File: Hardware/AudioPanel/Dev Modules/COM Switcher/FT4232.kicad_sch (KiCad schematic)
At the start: 81 parts, among them J601 PC1_COM, J602 PC2_COM, J603 PC3_COM, J604 PC4_COM, J605 2.54mm, Q601 BCM857BS, U601 FT4232H, U602 93LCxxA, Y601 12MHz

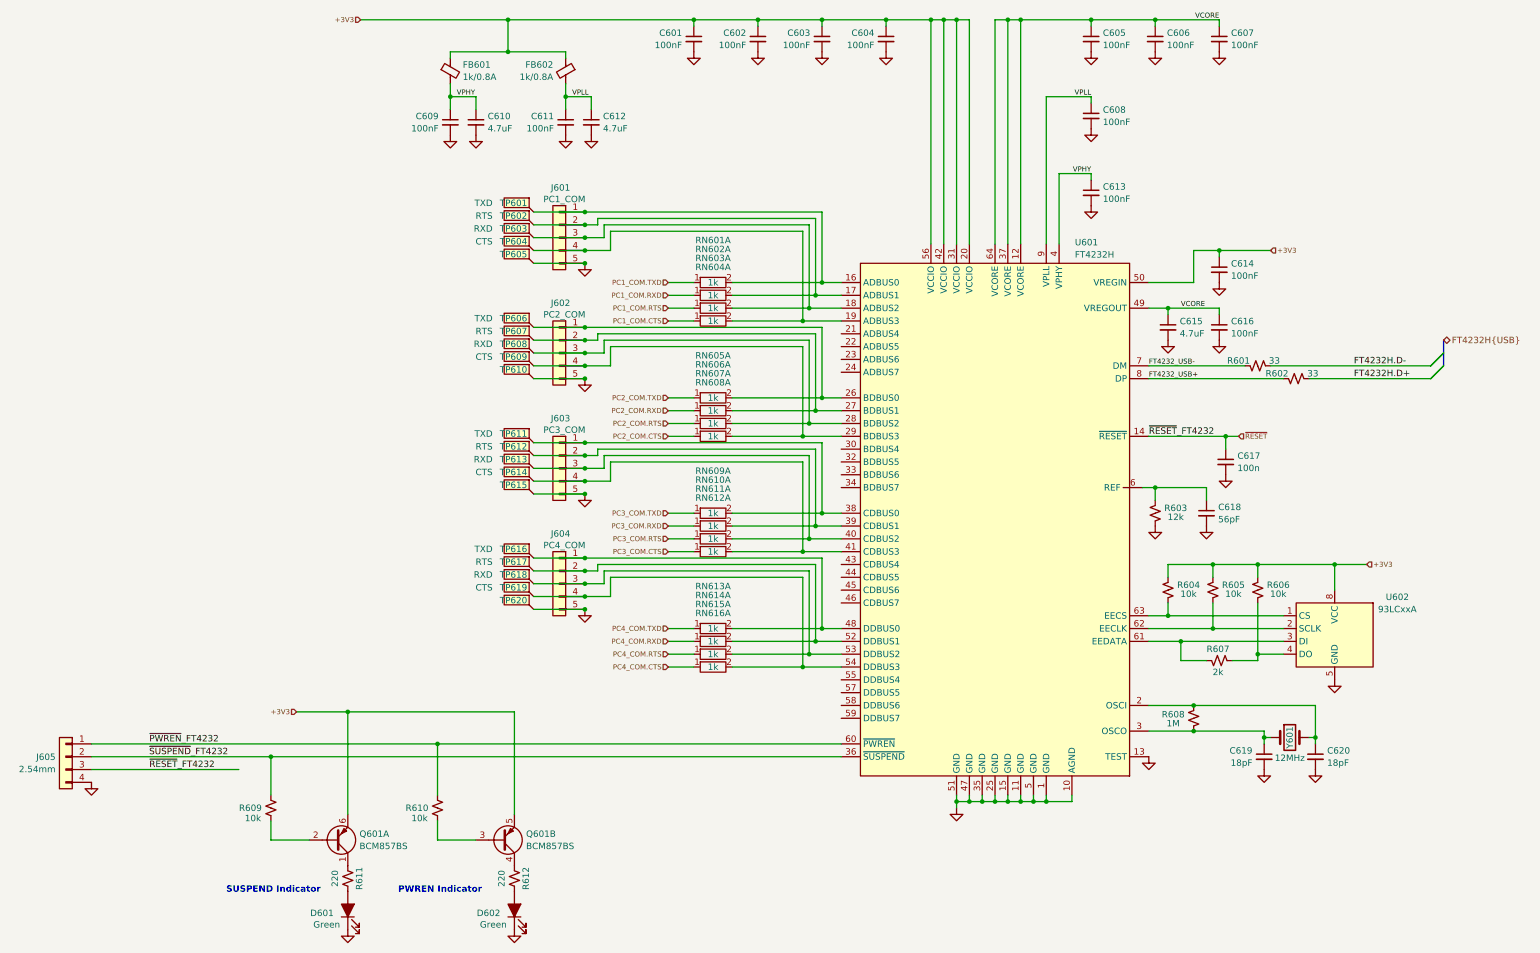
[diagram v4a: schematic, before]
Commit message: Changed passives to Worthington footprints
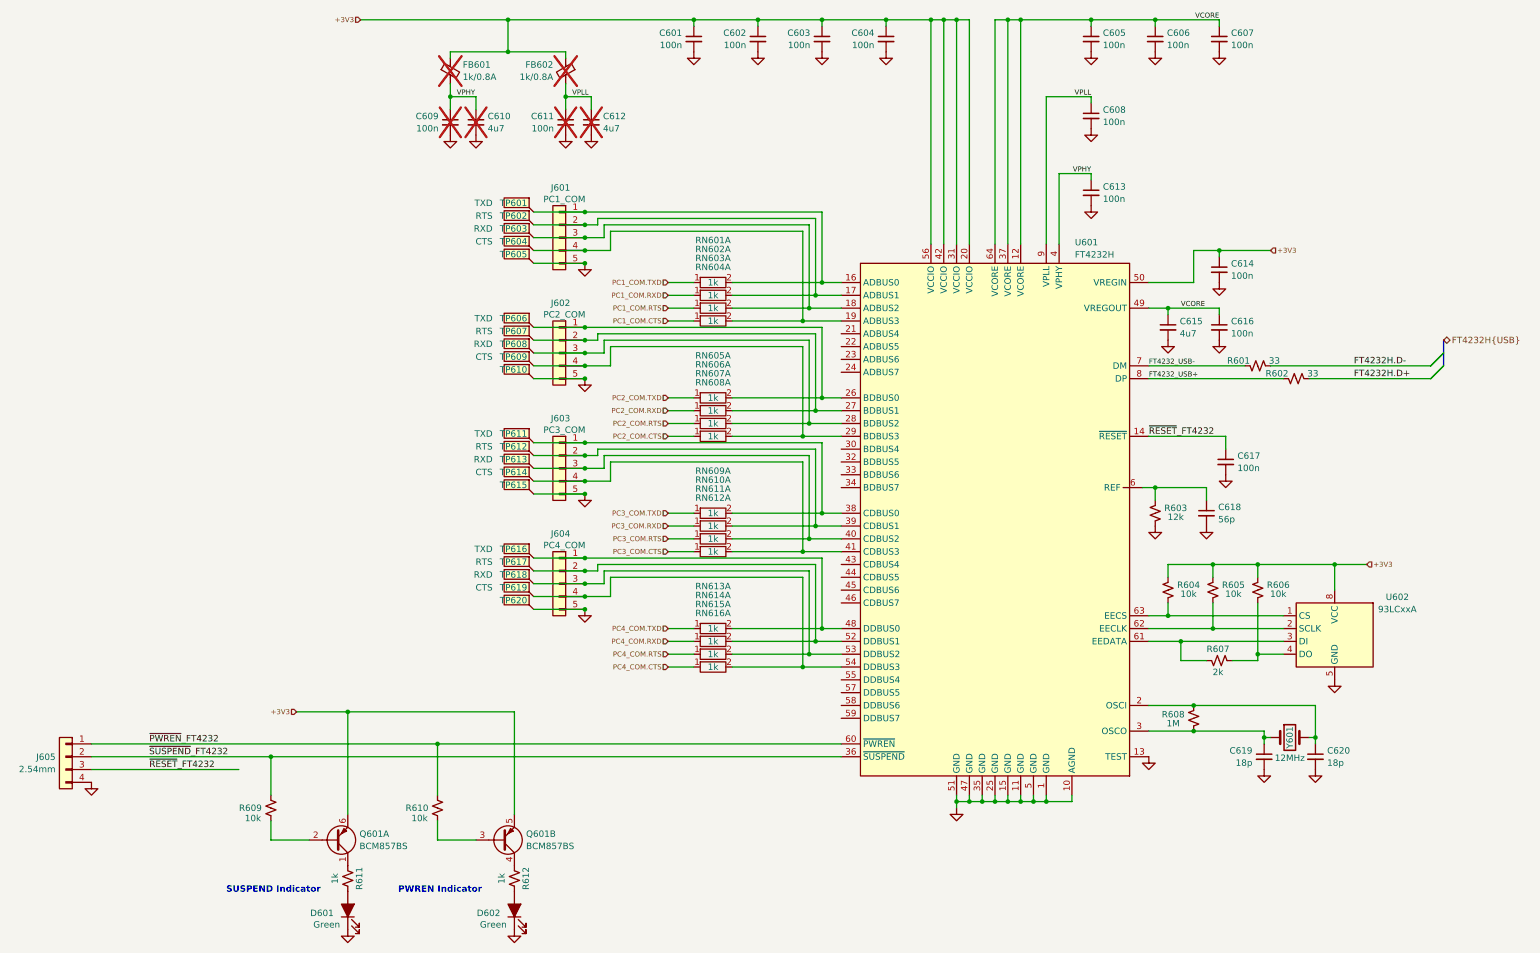
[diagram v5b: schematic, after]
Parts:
- C601, C602, C603, C604, C605, C606, C607, C608, C613, C614, C616: value 100nF -> 100n; footprint Capacitor_SMD:C_0402_1005Metric -> Libraries:Worthington_C_0402
- C609, C611: value 100nF -> 100n; footprint Capacitor_SMD:C_0402_1005Metric -> Libraries:Worthington_C_0402; now not fitted
- C610: value 4.7uF -> 4u7; footprint Capacitor_SMD:C_0603_1608Metric -> Libraries:Worthington_C_0603; now not fitted
- C612: value 4.7uF -> 4u7; footprint Capacitor_SMD:C_0603_1608Metric -> Libraries:Worthington_C_0402; now not fitted
- C615: value 4.7uF -> 4u7; footprint Capacitor_SMD:C_0603_1608Metric -> Libraries:Worthington_C_0603
- C617: footprint Capacitor_SMD:C_0402_1005Metric -> Libraries:Worthington_C_0402
- C618: value 56pF -> 56p; footprint Capacitor_SMD:C_0402_1005Metric -> Libraries:Worthington_C_0402
- C619, C620: value 18pF -> 18p; footprint Capacitor_SMD:C_0402_1005Metric -> Libraries:Worthington_C_0402
- FB601, FB602: now not fitted
- R601, R602, R603, R604, R605, R606, R607, R608, R609, R610: footprint Resistor_SMD:R_0402_1005Metric -> Libraries:Worthington_R_0402
- R611, R612: value 220 -> 1k; footprint Resistor_SMD:R_0402_1005Metric -> Libraries:Worthington_R_0402
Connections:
- net ~{RESET} renamed ~{RESET}_FT4232
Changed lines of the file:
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@@
 	)
 	(junction
-		(at 323.85 115.57)
-		(diameter 0)
-		(color 0 0 0 0)
-	)
-	(junction
 		(at 322.58 78.74)
 		(diameter 0)
@@
 	(wire
 		(pts
-			(xy 326.39 115.57) (xy 323.85 115.57)
-		)
-		(stroke
-			(width 0)
-			(type default)
-		)
-	)
-	(wire
-		(pts
 			(xy 256.54 33.02) (xy 265.43 33.02)
 		)
@@
 		)
 	)
-	(hierarchical_label "~{RESET}"
-		(shape input)
-		(at 326.39 115.57 0)
-		(effects
-			(font
-				(size 1 1)
-			)
-			(justify left)
-		)
-	)
 	(hierarchical_label "PC3_COM.TXD"
 		(shape input)
@@
 			)
 		)
-		(property "Footprint" "Resistor_SMD:R_0402_1005Metric"
+		(property "Footprint" "Libraries:Worthington_R_0402"
 			(at 312.42 146.05 0)
 			(effects
@@
 			)
 		)
-		(property "Footprint" "Resistor_SMD:R_0402_1005Metric"
+		(property "Footprint" "Libraries:Worthington_R_0402"
 			(at 321.31 146.05 0)
 			(effects
@@
 			)
 		)
-		(property "Value" "100nF"
+		(property "Value" "100n"
 			(at 216.1159 38.0484 0)
 			(effects
@@
 			)
 		)
-		(property "Footprint" "Capacitor_SMD:C_0402_1005Metric"
+		(property "Footprint" "Libraries:Worthington_C_0402"
 			(at 218.44 36.83 0)
 			(effects
@@
 			)
 		)
-		(property "Value" "100nF"
+		(property "Value" "100n"
 			(at 228.8159 38.0484 0)
 			(effects
@@
 			)
 		)
-		(property "Footprint" "Capacitor_SMD:C_0402_1005Metric"
+		(property "Footprint" "Libraries:Worthington_C_0402"
 			(at 231.14 36.83 0)
 			(effects
@@
 		(in_bom yes)
 		(on_board yes)
-		(dnp no)
+		(dnp yes)
 		(fields_autoplaced yes)
 		(property "Reference" "FB601"
@@
 			)
 		)
-		(property "Footprint" "Resistor_SMD:R_0402_1005Metric"
+		(property "Footprint" "Libraries:Worthington_R_0402"
 			(at 167.64 189.23 0)
 			(effects
@@
 			)
 		)
-		(property "Value" "220"
+		(property "Value" "1k"
 			(at 147.32 203.2 90)
 			(effects
@@
 			)
 		)
-		(property "Footprint" "Resistor_SMD:R_0402_1005Metric"
+		(property "Footprint" "Libraries:Worthington_R_0402"
 			(at 149.86 203.2 0)
 			(effects
@@
 		(in_bom yes)
 		(on_board yes)
-		(dnp no)
+		(dnp yes)
 		(property "Reference" "C610"
 			(at 177.5841 52.1341 0)
@@
 			)
 		)
-		(property "Value" "4.7uF"
+		(property "Value" "4u7"
 			(at 177.5841 54.5584 0)
 			(effects
@@
 			)
 		)
-		(property "Footprint" "Capacitor_SMD:C_0603_1608Metric"
+		(property "Footprint" "Libraries:Worthington_C_0603"
 			(at 175.26 53.34 0)
 			(effects
@@
 			)
 		)
-		(property "Value" "100nF"
+		(property "Value" "100n"
 			(at 324.9041 95.1984 0)
 			(effects
@@
 			)
 		)
-		(property "Footprint" "Capacitor_SMD:C_0402_1005Metric"
+		(property "Footprint" "Libraries:Worthington_C_0402"
 			(at 322.58 93.98 0)
 			(effects
@@
 			)
 		)
-		(property "Value" "18pF"
+		(property "Value" "18p"
 			(at 343.9541 180.2884 0)
 			(effects
@@
 			)
 		)
-		(property "Footprint" "Capacitor_SMD:C_0402_1005Metric"
+		(property "Footprint" "Libraries:Worthington_C_0402"
 			(at 341.63 179.07 0)
 			(effects
@@
 			)
 		)
-		(property "Footprint" "Resistor_SMD:R_0402_1005Metric"
+		(property "Footprint" "Libraries:Worthington_R_0402"
 			(at 337.82 104.14 0)
 			(effects
@@
 		(in_bom yes)
 		(on_board yes)
-		(dnp no)
+		(dnp yes)
 		(property "Reference" "C611"
 			(at 190.7159 52.1341 0)
@@
 			)
 		)
-		(property "Value" "100nF"
+		(property "Value" "100n"
 			(at 190.7159 54.5584 0)
 			(effects
@@
 			)
 		)
-		(property "Footprint" "Capacitor_SMD:C_0402_1005Metric"
+		(property "Footprint" "Libraries:Worthington_C_0402"
 			(at 193.04 53.34 0)
 			(effects
@@
 			)
 		)
-		(property "Footprint" "Resistor_SMD:R_0402_1005Metric"
+		(property "Footprint" "Libraries:Worthington_R_0402"
 			(at 309.88 130.81 0)
 			(effects
@@
 			)
 		)
-		(property "Footprint" "Capacitor_SMD:C_0402_1005Metric"
+		(property "Footprint" "Libraries:Worthington_C_0402"
 			(at 323.85 120.65 0)
 			(effects
@@
 			)
 		)
-		(property "Footprint" "Resistor_SMD:R_0402_1005Metric"
+		(property "Footprint" "Libraries:Worthington_R_0402"
 			(at 317.5 171.45 0)
 			(effects
@@
 			)
 		)
-		(property "Footprint" "Resistor_SMD:R_0402_1005Metric"
+		(property "Footprint" "Libraries:Worthington_R_0402"
 			(at 330.2 146.05 0)
 			(effects
@@
 		(in_bom yes)
 		(on_board yes)
-		(dnp no)
+		(dnp yes)
 		(property "Reference" "C609"
 			(at 167.8559 52.1341 0)
@@
 			)
 		)
-		(property "Value" "100nF"
+		(property "Value" "100n"
 			(at 167.8559 54.5584 0)
 			(effects
@@
 			)
 		)
-		(property "Footprint" "Capacitor_SMD:C_0402_1005Metric"
+		(property "Footprint" "Libraries:Worthington_C_0402"
 			(at 170.18 53.34 0)
 			(effects
@@
 			)
 		)
-		(property "Value" "56pF"
+		(property "Value" "56p"
 			(at 322.3641 132.0284 0)
 			(effects
@@
 			)
 		)
-		(property "Footprint" "Capacitor_SMD:C_0402_1005Metric"
+		(property "Footprint" "Libraries:Worthington_C_0402"
 			(at 320.04 130.81 0)
 			(effects
@@
 			)
 		)
-		(property "Value" "4.7uF"
+		(property "Value" "4u7"
 			(at 314.7441 95.1984 0)
 			(effects
@@
 			)
 		)
-		(property "Footprint" "Capacitor_SMD:C_0603_1608Metric"
+		(property "Footprint" "Libraries:Worthington_C_0603"
 			(at 312.42 93.98 0)
 			(effects
@@
 			)
 		)
-		(property "Footprint" "Resistor_SMD:R_0402_1005Metric"
+		(property "Footprint" "Libraries:Worthington_R_0402"
 			(at 330.2 101.6 0)
 			(effects
@@
 			)
 		)
-		(property "Value" "220"
+		(property "Value" "1k"
 			(at 180.34 203.2 90)
 			(effects
@@
 			)
 		)
-		(property "Footprint" "Resistor_SMD:R_0402_1005Metric"
+		(property "Footprint" "Libraries:Worthington_R_0402"
 			(at 182.88 203.2 0)
 			(effects
@@
 			)
 		)
-		(property "Value" "18pF"
+		(property "Value" "18p"
 			(at 329.1459 180.2884 0)
 			(effects
@@
 			)
 		)
-		(property "Footprint" "Capacitor_SMD:C_0402_1005Metric"
+		(property "Footprint" "Libraries:Worthington_C_0402"
 			(at 331.47 179.07 0)
 			(effects
@@
 			)
 		)
-		(property "Footprint" "Resistor_SMD:R_0402_1005Metric"
+		(property "Footprint" "Libraries:Worthington_R_0402"
 			(at 134.62 189.23 0)
 			(effects
@@
 			)
 		)
-		(property "Value" "100nF"
+		(property "Value" "100n"
 			(at 299.5041 38.0484 0)
 			(effects
@@
 			)
 		)
-		(property "Footprint" "Capacitor_SMD:C_0402_1005Metric"
+		(property "Footprint" "Libraries:Worthington_C_0402"
 			(at 297.18 36.83 0)
 			(effects
@@
 			)
 		)
-		(property "Value" "100nF"
+		(property "Value" "100n"
 			(at 241.5159 38.0484 0)
 			(effects
@@
 			)
 		)
-		(property "Footprint" "Capacitor_SMD:C_0402_1005Metric"
+		(property "Footprint" "Libraries:Worthington_C_0402"
 			(at 243.84 36.83 0)
 			(effects
@@
 			)
 		)
-		(property "Value" "100nF"
+		(property "Value" "100n"
 			(at 299.5041 68.5284 0)
 			(effects
@@
 			)
 		)
-		(property "Footprint" "Capacitor_SMD:C_0402_1005Metric"
+		(property "Footprint" "Libraries:Worthington_C_0402"
 			(at 297.18 67.31 0)
 			(effects
@@
 		(in_bom yes)
 		(on_board yes)
-		(dnp no)
+		(dnp yes)
 		(property "Reference" "C612"
 			(at 200.4441 52.1341 0)
@@
 			)
 		)
-		(property "Value" "4.7uF"
+		(property "Value" "4u7"
 			(at 200.4441 54.5584 0)
 			(effects
@@
 			)
 		)
-		(property "Footprint" "Capacitor_SMD:C_0603_1608Metric"
+		(property "Footprint" "Libraries:Worthington_C_0402"
 			(at 198.12 53.34 0)
 			(effects
@@
 			)
 		)
-		(property "Value" "100nF"
+		(property "Value" "100n"
 			(at 324.9041 83.7684 0)
 			(effects
@@
 			)
 		)
-		(property "Footprint" "Capacitor_SMD:C_0402_1005Metric"
+		(property "Footprint" "Libraries:Worthington_C_0402"
 			(at 322.58 82.55 0)
 			(effects
@@
 			)
 		)
-		(property "Value" "100nF"
+		(property "Value" "100n"
 			(at 324.9041 38.0484 0)
 			(effects
@@
 			)
 		)
-		(property "Footprint" "Capacitor_SMD:C_0402_1005Metric"
+		(property "Footprint" "Libraries:Worthington_C_0402"
 			(at 322.58 36.83 0)
 			(effects
@@
 		(in_bom yes)
 		(on_board yes)
-		(dnp no)
+		(dnp yes)
 		(property "Reference" "FB602"
 			(at 190.5762 41.9297 0)
@@
 			)
 		)
-		(property "Value" "100nF"
+		(property "Value" "100n"
 			(at 299.5041 53.2884 0)
 			(effects
@@
 			)
 		)
-		(property "Footprint" "Capacitor_SMD:C_0402_1005Metric"
+		(property "Footprint" "Libraries:Worthington_C_0402"
 			(at 297.18 52.07 0)
 			(effects
@@
 			)
 		)
-		(property "Value" "100nF"
+		(property "Value" "100n"
 			(at 312.2041 38.0484 0)
 			(effects
@@
 			)
 		)
-		(property "Footprint" "Capacitor_SMD:C_0402_1005Metric"
+		(property "Footprint" "Libraries:Worthington_C_0402"
 			(at 309.88 36.83 0)
 			(effects
@@
 			)
 		)
-		(property "Footprint" "Resistor_SMD:R_0402_1005Metric"
+		(property "Footprint" "Libraries:Worthington_R_0402"
 			(at 322.58 160.02 0)
 			(effects
@@
 			)
 		)
-		(property "Value" "100nF"
+		(property "Value" "100n"
 			(at 254.2159 38.0484 0)
 			(effects
@@
 			)
 		)
-		(property "Footprint" "Capacitor_SMD:C_0402_1005Metric"
+		(property "Footprint" "Libraries:Worthington_C_0402"
 			(at 256.54 36.83 0)
 			(effects

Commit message: Added more LEDs
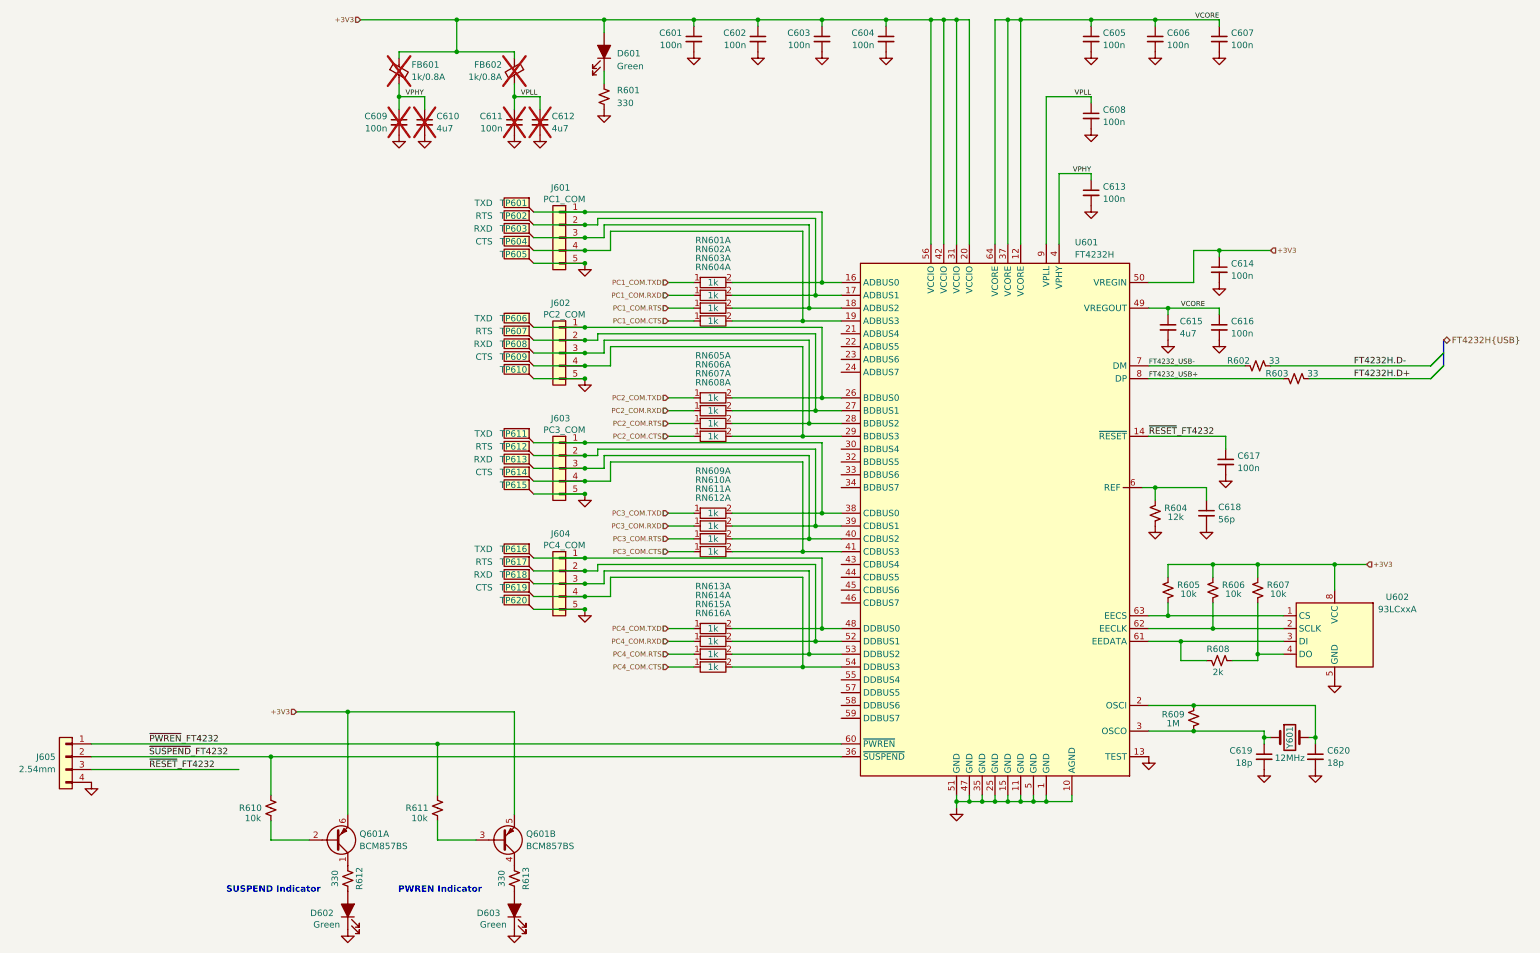
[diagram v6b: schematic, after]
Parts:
- added D601: Green, LED_THT:LED_D5.0mm, symbol Device:LED_Filled
- added R601: 330, Libraries:Worthington_R_0603, symbol Device:R_Small_US
- R612: renamed from R611; value 1k -> 330
- R613: renamed from R612; value 1k -> 330
- renumbered D601 to D602, D602 to D603, R601 to R602, R602 to R603, R603 to R604, R604 to R605, R605 to R606, R606 to R607, R607 to R608, R608 to R609, R609 to R610, R610 to R611
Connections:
- net +3V3: now also D601.2 (A)
- net GND: now also R601.1
- new net: D601.1 (K), R601.2
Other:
- moved on the sheet: C609, C610, C611, C612, FB601, FB602

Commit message: Resized some resistors
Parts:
- R601: footprint Libraries:Worthington_R_0603 -> Libraries:Worthington_R_0402
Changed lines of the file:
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@@
 			)
 		)
-		(property "Footprint" "Libraries:Worthington_R_0603"
+		(property "Footprint" "Libraries:Worthington_R_0402"
 			(at 200.66 48.26 0)
 			(effects
